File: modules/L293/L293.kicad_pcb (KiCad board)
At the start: 2 copper layers, 40.6 x 40.6 mm, 37 parts, among them J1 2, J10 11, J11 12, J12 13, J13 A0, J14 A1, J15 A2, J16 A3, J17 A4, J18 A5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

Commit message: Add photomask in pdf. Add gerber.
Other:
- board text added: "09.03.2020"
- board text removed: "04.03.2020"
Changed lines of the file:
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@@
     (nets 30)
   )
-  (page A4)
+  (page A4 portrait)
   (layers
     (0 F.Cu signal)
@@
     (visible_elements 7FFFFFFF)
     (pcbplotparams
-      (layerselection 0x010fc_ffffffff)
+      (layerselection 0x00000_7fffffff)
       (usegerberextensions false)
       (usegerberattributes false)
@@
       (hpglpenspeed 20)
       (hpglpendiameter 15.000000)
-      (psnegative false)
+      (psnegative true)
       (psa4output false)
       (plotreference true)
@@
       (padsonsilk false)
       (subtractmaskfromsilk false)
-      (outputformat 1)
-      (mirror false)
+      (outputformat 4)
+      (mirror true)
       (drillshape 1)
       (scaleselection 1)
-      (outputdirectory ""))
+      (outputdirectory "l293/"))
   )
   (net 0 "")
@@
   )
   (gr_poly (pts (xy 113.35 60.6) (xy 114.06 61.62) (xy 114.28 61.94) (xy 114.47 62.12) (xy 114.53 62.16) (xy 114.96 62.29) (xy 115 62.27) (xy 115 62.18) (xy 114.81 61.75) (xy 114.51 61.1) (xy 115.32 62.09) (xy 115.52 62.31) (xy 115.64 62.41) (xy 115.72 62.44) (xy 115.9 62.45) (xy 116.12 62.51) (xy 116.08 62.39) (xy 115.57 61.5) (xy 116.34 62.34) (xy 116.5 62.53) (xy 116.59 62.61) (xy 116.7 62.66) (xy 117.14 62.71) (xy 117.6 62.73) (xy 118.08 62.13) (xy 118.23 61.98) (xy 118.22 62.06) (xy 118.08 62.39) (xy 118 62.56) (xy 117.99 62.64) (xy 118.07 62.65) (xy 118.47 62.63) (xy 118.82 62.52) (xy 119.49 61.95) (xy 119.37 62.24) (xy 118.94 62.89) (xy 118.61 62.95) (xy 118 63) (xy 117.81 63.07) (xy 118.03 63.13) (xy 119.36 63.35) (xy 119.68 63.42) (xy 119.81 63.52) (xy 119.83 63.69) (xy 119.81 63.85) (xy 119.75 63.93) (xy 119.7 63.95) (xy 119.66 64.03) (xy 119.66 64.13) (xy 119.6 64.18) (xy 119.41 64.23) (xy 118.79 64.34) (xy 118.5 64.42) (xy 118.37 64.54) (xy 118.34 64.6) (xy 118.31 64.75) (xy 118.32 64.92) (xy 117.99 68.69) (xy 118.04 65.3) (xy 118.03 65.02) (xy 118.02 64.83) (xy 118.01 64.79) (xy 117.97 64.75) (xy 117.92 64.87) (xy 117.89 65.2) (xy 117.86 65.69) (xy 117.83 67.07) (xy 117.81 67.6) (xy 117.77 67.93) (xy 117.74 67.75) (xy 117.71 67.07) (xy 117.71 66.19) (xy 117.69 64.97) (xy 117.53 65.01) (xy 117.42 65.01) (xy 117.35 64.96) (xy 117.28 64.83) (xy 117.04 64.2) (xy 117.35 63.8) (xy 117.31 64.03) (xy 117.3 64.19) (xy 117.3 64.26) (xy 117.37 64.39) (xy 117.52 64.6) (xy 118.43 64.21) (xy 118.56 64.14) (xy 118.61 64.08) (xy 118.5 64.04) (xy 118.71 64) (xy 119.23 63.99) (xy 119.35 63.97) (xy 119.44 63.92) (xy 119.47 63.86) (xy 119.44 63.74) (xy 119.28 63.64) (xy 119.01 63.53) (xy 118.61 63.45) (xy 118.37 63.44) (xy 118.23 63.46) (xy 118.18 63.5) (xy 118.11 63.6) (xy 118.06 63.61) (xy 118 63.61) (xy 117.88 63.56) (xy 117.73 63.46) (xy 117.69 63.4) (xy 117.68 63.36) (xy 117.62 63.33) (xy 117.54 63.3) (xy 117.05 63.28) (xy 116.6 63.29) (xy 116.46 63.31) (xy 116.34 63.34) (xy 116.36 63.38) (xy 116.57 63.42) (xy 116.87 63.44) (xy 117.38 63.45) (xy 116.96 63.6) (xy 116.96 63.63) (xy 117.16 63.65) (xy 117.17 63.68) (xy 116.93 63.8) (xy 116.87 63.87) (xy 116.74 64.06) (xy 116.54 64.49) (xy 116.11 65.54) (xy 115.89 66.19) (xy 115.84 66.36) (xy 115.81 66.5) (xy 115.86 66.58) (xy 115.91 66.55) (xy 115.95 66.48) (xy 116.04 66.26) (xy 116.22 65.75) (xy 116.53 64.92) (xy 116.49 65.18) (xy 116.24 66.18) (xy 116.18 66.39) (xy 116.12 66.73) (xy 116.1 66.85) (xy 116.1 66.96) (xy 116.15 67.02) (xy 116.21 66.94) (xy 116.25 66.79) (xy 116.35 66.42) (xy 116.51 65.7) (xy 116.54 65.7) (xy 116.39 66.86) (xy 116.32 67.31) (xy 116.71 67.88) (xy 116.87 68.18) (xy 116.26 67.47) (xy 115.56 66.58) (xy 113.92 66.65) (xy 115.32 66.35) (xy 115.53 66.28) (xy 115.61 66.06) (xy 115.9 65.18) (xy 116.15 64.33) (xy 116.31 63.66) (xy 115.58 63.09) (xy 115.94 63.05) (xy 116.39 63.07) (xy 116.87 63.08) (xy 114.95 62.66) (xy 114.15 62.47) (xy 113.72 61.5)) (layer F.SilkS) (width 0.1))
-  (gr_text 04.03.2020 (at 118.15 61.18) (layer F.Cu)
+  (gr_text 09.03.2020 (at 117.45 61.19) (layer F.Cu)
     (effects (font (size 1 0.8) (thickness 0.15)))
   )

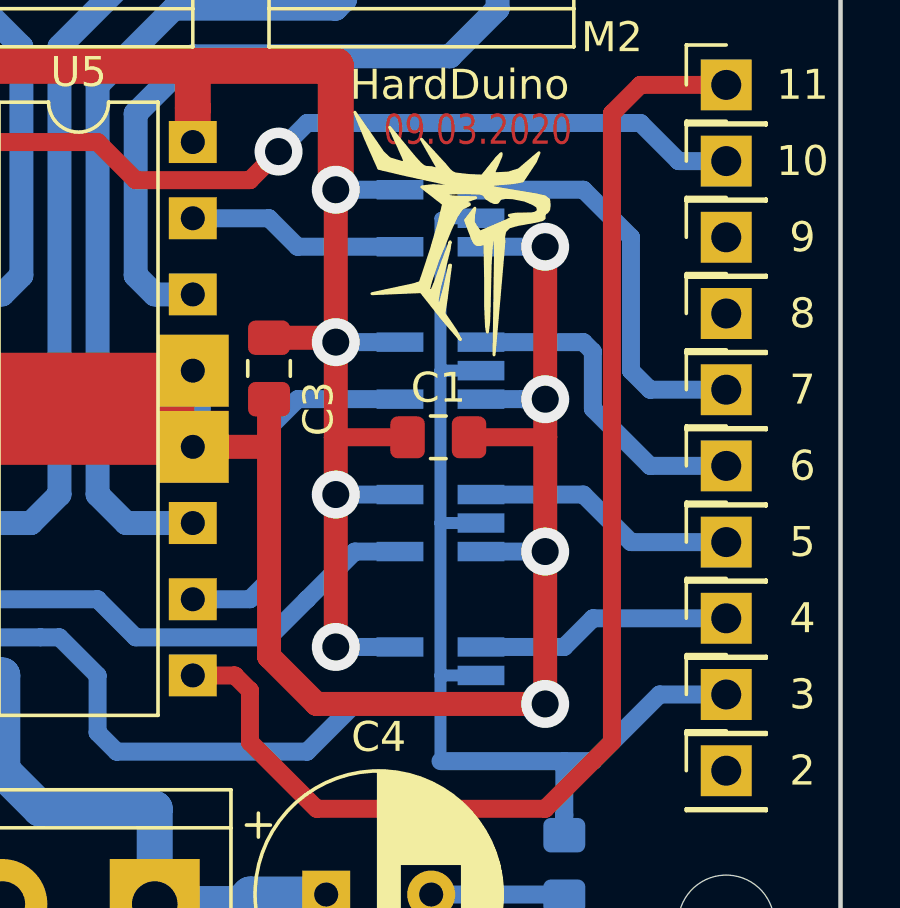
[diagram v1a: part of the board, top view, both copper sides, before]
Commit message: Replace SOT23-5 to TSSOP5
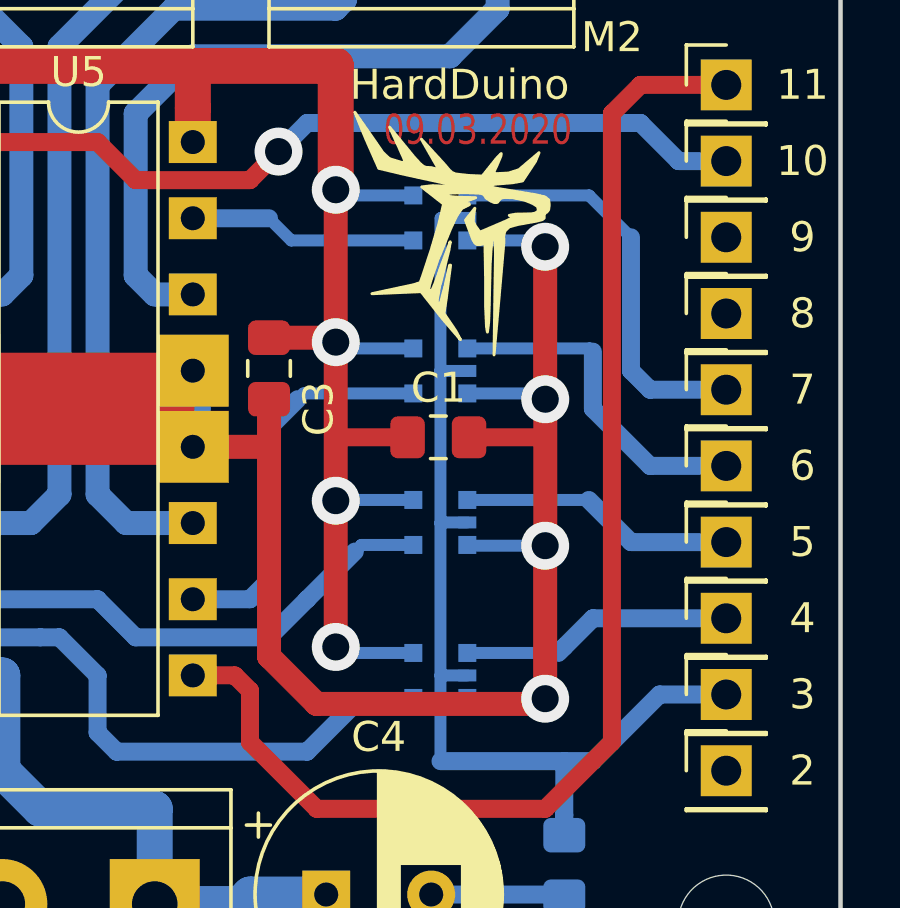
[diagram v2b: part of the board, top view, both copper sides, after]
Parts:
- U1, U2, U3, U4: footprint Package_TO_SOT_SMD:SOT-23-5_HandSoldering -> CommonLibrary:tssop5
- moved U2 3.29 mm to (119.0, 72.7), turned to 270 degrees
- moved U4 3.28 mm to (119.0, 62.5), turned to 270 degrees
- moved U1 3.28 mm to (119.0, 77.8), turned to 270 degrees
- moved U3 3.27 mm to (119.0, 67.6), turned to 270 degrees
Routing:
- net VCC: track 55.4 -> 57.5 mm
- net GND: track 123.3 -> 125.3 mm
- net Net-(J2-Pad1): track 36.4 -> 34.6 mm
- net Net-(J3-Pad1): track 8.57 -> 9.11 mm
- net Net-(U2-Pad4): track 16.2 -> 16.8 mm
- net Net-(U1-Pad4): track 36.2 -> 36.7 mm
- net Net-(U3-Pad4): track 12.6 -> 13.2 mm

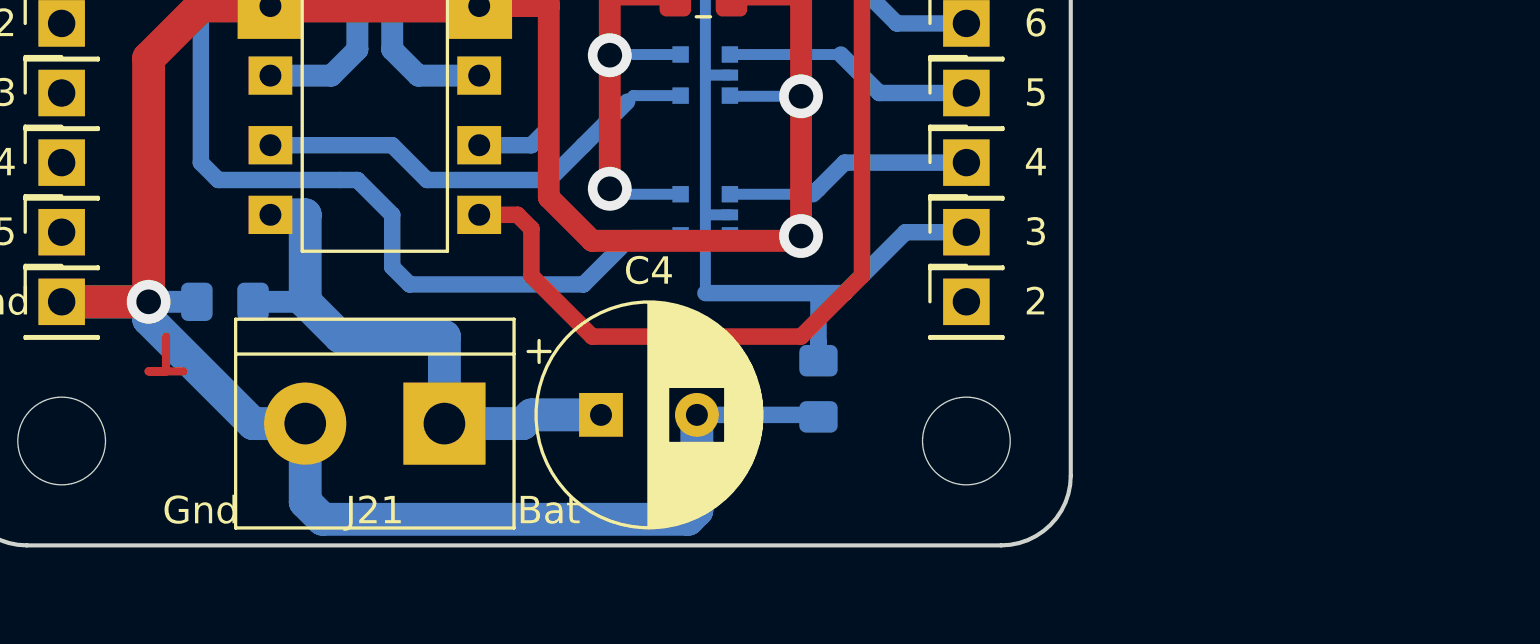
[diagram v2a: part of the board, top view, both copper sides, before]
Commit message: Add L4940 to motor shield
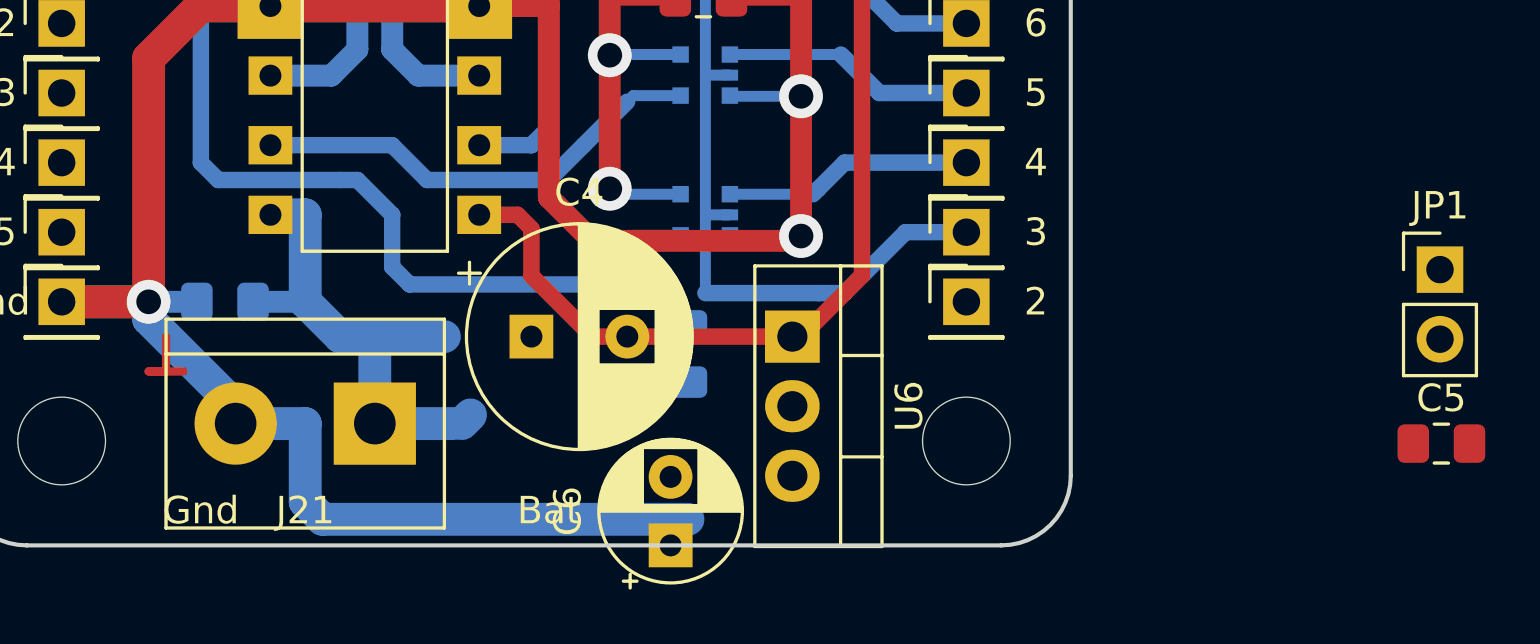
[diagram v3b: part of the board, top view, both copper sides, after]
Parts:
- added C5: 0,1uF, Capacitor_SMD:C_0805_2012Metric_Pad1.15x1.40mm_HandSolder, F.Cu at (143.1, 87.7)
- added C6: 22uF, Capacitor_THT:CP_Radial_D5.0mm_P2.50mm, F.Cu at (114.9, 91.4)
- added JP1: Jumper_2_Open, Connector_PinHeader_2.54mm:PinHeader_1x02_P2.54mm_Vertical, F.Cu at (143.0, 81.4)
- added U6: L4940, Package_TO_SOT_THT:TO-220-3_Vertical, F.Cu at (119.4, 83.8)
- moved R1 4.93 mm to (115.6, 84.5)
- moved C4 3.82 mm to (109.9, 83.8)
- moved J21 2.54 mm to (104.1, 87.0)
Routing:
- net GND: track 125.3 -> 116.9 mm
- net Net-(C2-Pad2): track 21.0 -> 18.4 mm
- net Net-(J2-Pad1): track 34.6 -> 32.1 mm

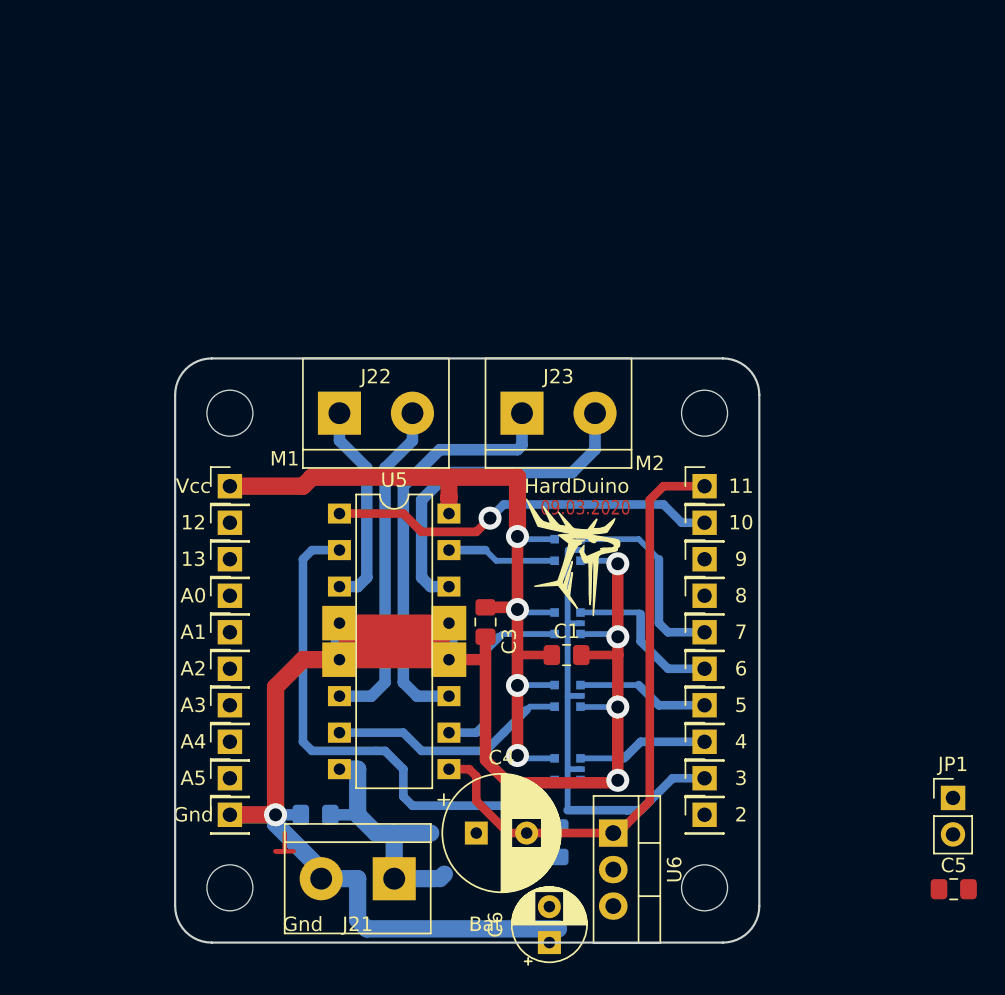
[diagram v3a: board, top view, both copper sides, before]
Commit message: Add stab to motor shield
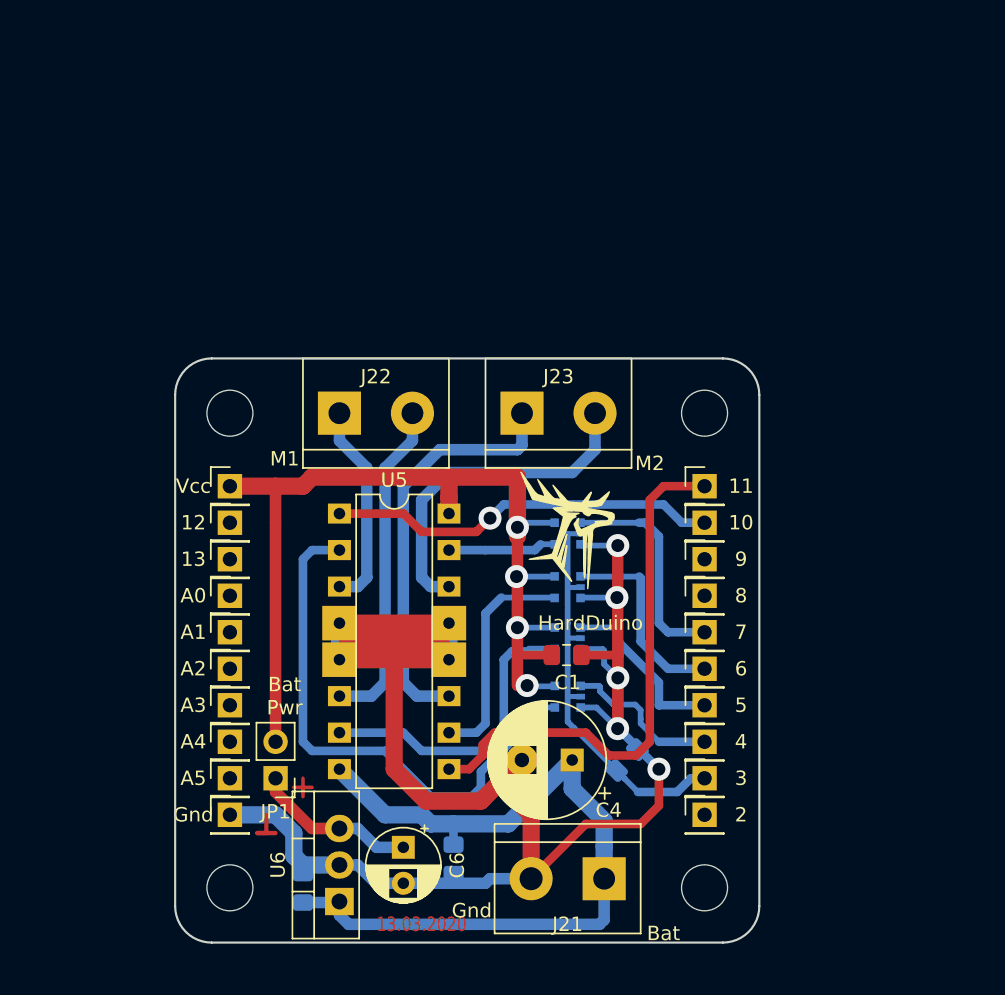
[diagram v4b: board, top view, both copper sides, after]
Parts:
- removed C3: 0.1uF, Capacitor_SMD:C_0805_2012Metric_Pad1.15x1.40mm_HandSolder
- C5: moved to B.Cu
- moved JP1 47.1 mm to (95.9, 80.0), turned to 180 degrees
- moved C5 45.3 mm to (97.8, 87.6), turned to 90 degrees
- moved U6 19.6 mm to (100.3, 88.6), turned to 90 degrees
- moved J21 14.6 mm to (118.7, 87.0)
- moved C6 12.1 mm to (104.8, 84.8), turned to 270 degrees
- moved C2 10.1 mm to (108.3, 85.7), turned to 90 degrees
- moved C4 8.38 mm to (116.5, 78.7), turned to 180 degrees
- moved R1 7.44 mm to (120.3, 78.7), turned to 225 degrees
- moved U1 5.04 mm to (119.1, 72.7)
- moved U2 4.01 mm to (119.0, 68.6)
- moved U3 2.51 mm to (119.0, 65.1)
- moved U4 1.15 mm to (119.0, 61.4)
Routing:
- net Net-(C2-Pad2): track 18.4 -> 55.4 mm
- net Net-(C6-Pad1): track 0.00 -> 11.4 mm
- net VCC: track 57.5 -> 67.2 mm
- net Net-(J10-Pad1): track 42.9 -> 37.6 mm
- net Net-(U2-Pad4): track 16.8 -> 21.4 mm
- net Net-(J2-Pad1): track 32.1 -> 28.5 mm
- net Net-(J4-Pad1): track 9.21 -> 12.2 mm
- net (no net): track 3.17 -> 5.72 mm
- net Net-(U3-Pad4): track 13.2 -> 15.7 mm
- net Net-(J5-Pad1): track 11.4 -> 13.9 mm
- net Net-(J3-Pad1): track 9.11 -> 11.0 mm
- net Net-(U1-Pad4): track 36.7 -> 38.4 mm
- net Net-(J6-Pad1): track 13.9 -> 15.3 mm
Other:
- board text added: "13.03.2020"
- board text added: "Bat Pwr"
- board text removed: "09.03.2020"

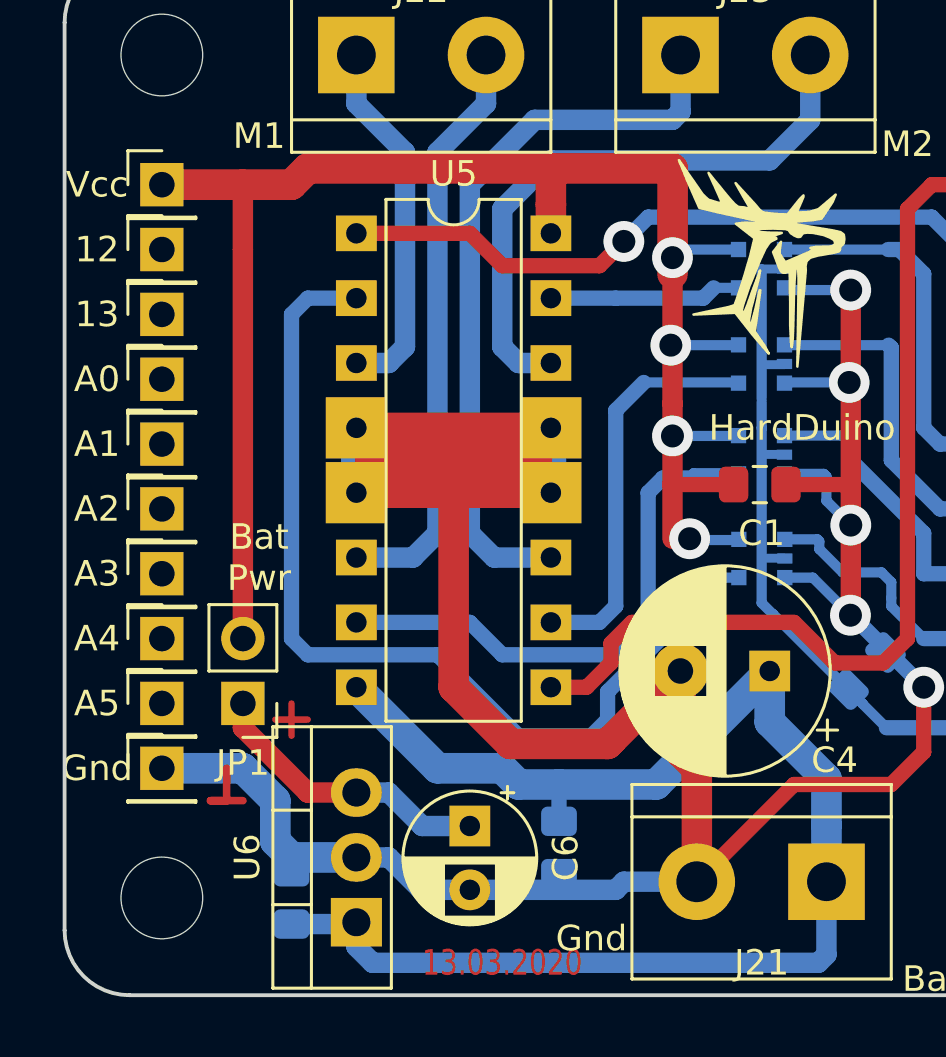
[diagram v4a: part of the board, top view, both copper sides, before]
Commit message: Small fixes L293
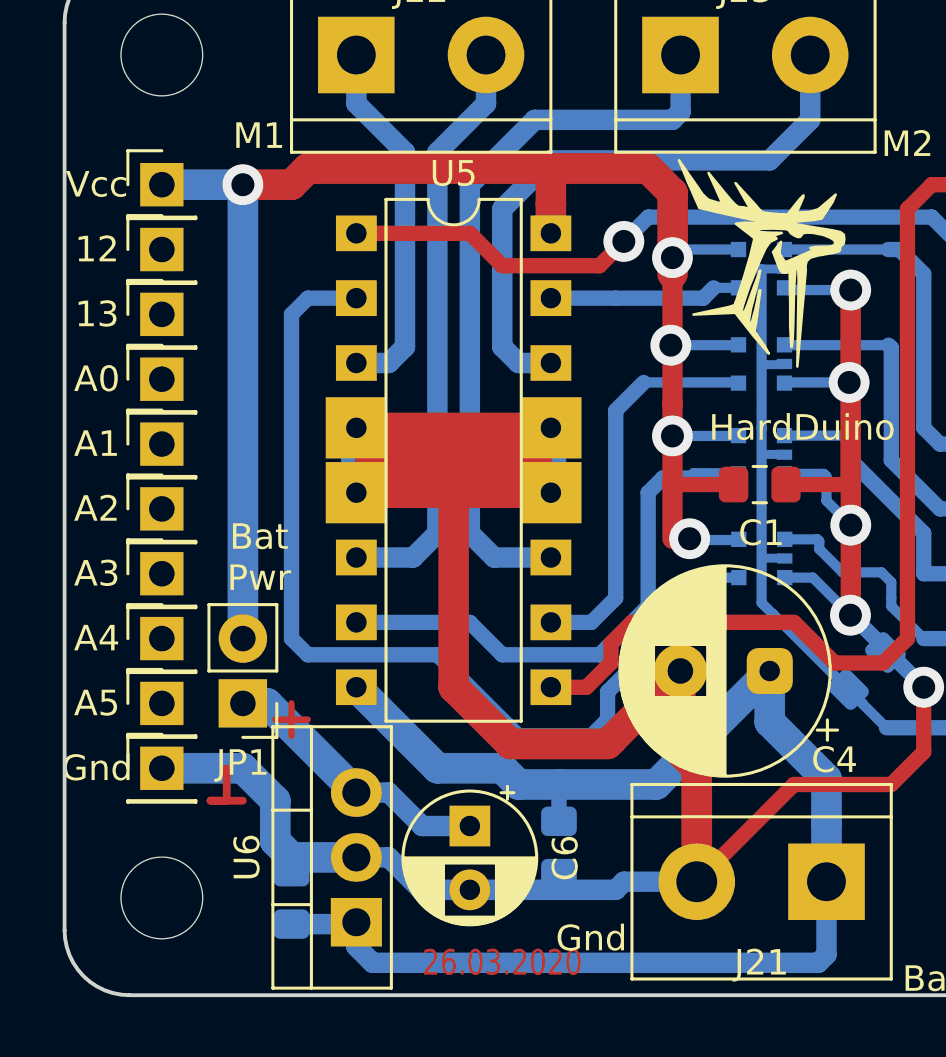
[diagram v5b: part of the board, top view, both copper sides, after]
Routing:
- net Net-(C6-Pad1): track 11.4 -> 10.9 mm
- net VCC: track 67.2 -> 66.6 mm, vias 4 -> 5
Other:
- board text added: "26.03.2020"
- board text removed: "13.03.2020"
